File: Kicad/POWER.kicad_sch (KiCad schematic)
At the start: 0 parts

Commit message: power section
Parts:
- added C? (x2): 10uF, symbol Device:C_Small
- added C? (x2): 1u, symbol Device:C_Small
- added R?: 10k, symbol Device:R_Small
- added U?: TPS76718QD, D0008A_N, symbol project_sym_lib:TPS76718QD
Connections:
- new net GND: C?.2, C?.2, C?.2, C?.2, U?.1 (GND), U?.2 (EN_N)
- new net VDD_1V8: C?.1, C?.1, R?.2, U?.5 (OUT), U?.6 (OUT)
- new net V_BUCK: C?.1, C?.1, U?.3 (IN), U?.4 (IN)
- new net ~{RESET}: R?.1, U?.8 (RESET_N)
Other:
- note removed: "TODO: LDO 3V3"

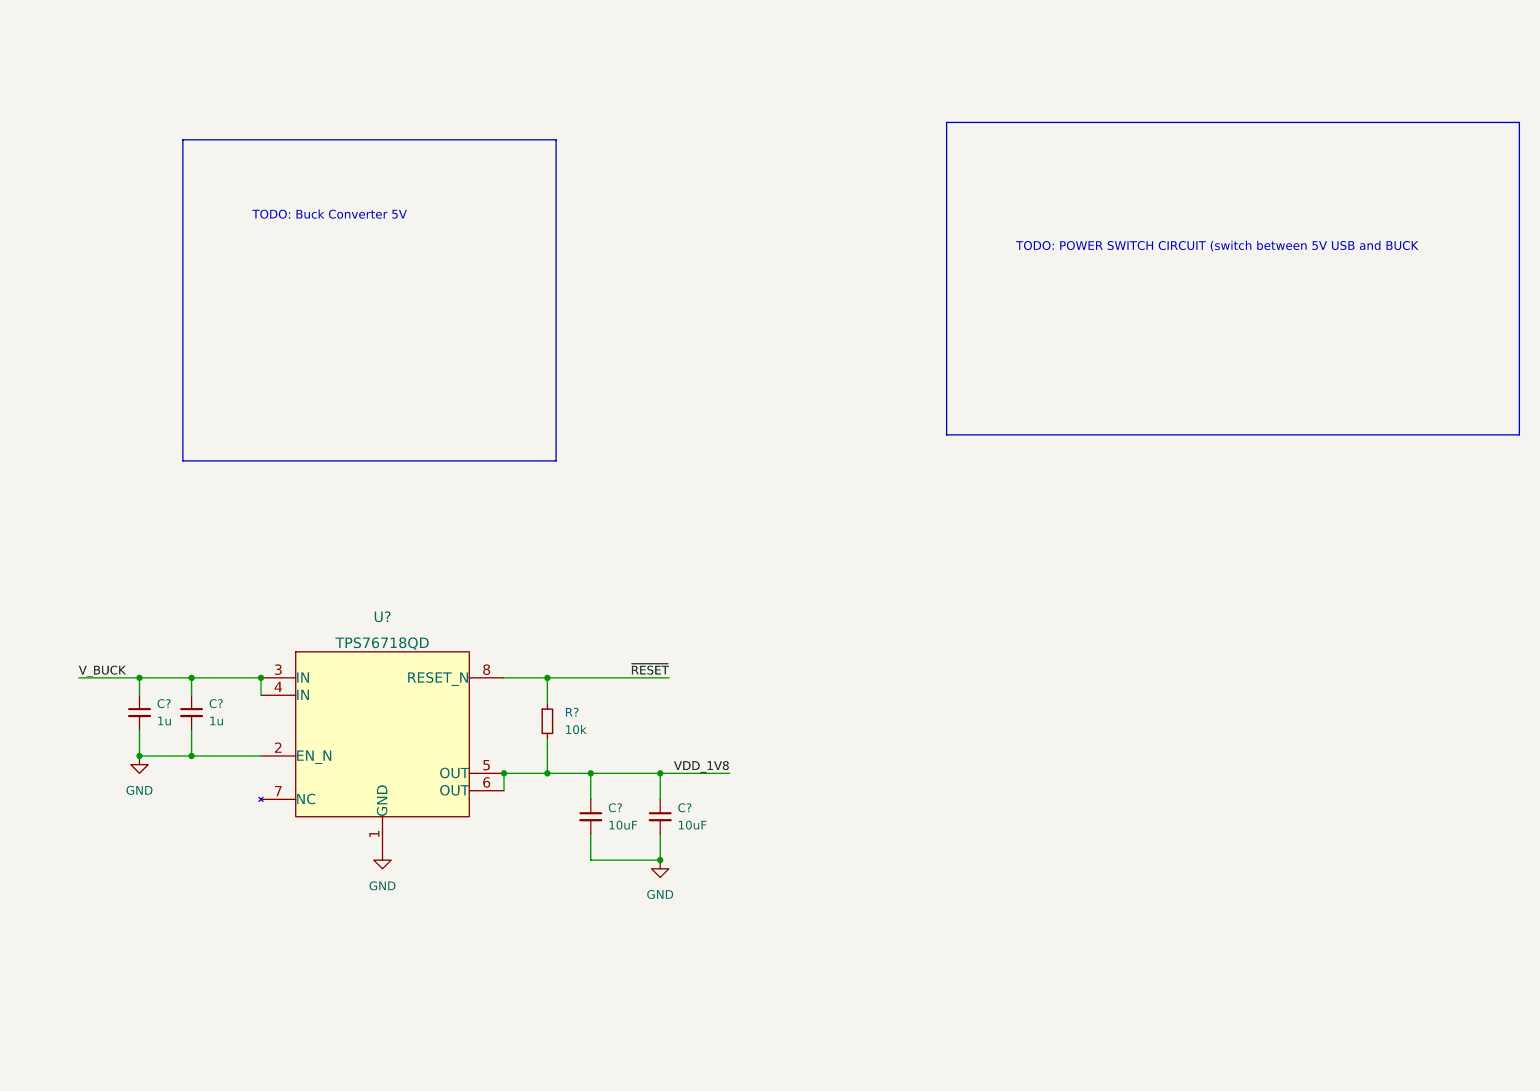
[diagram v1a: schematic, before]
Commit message: Basic Power layout done
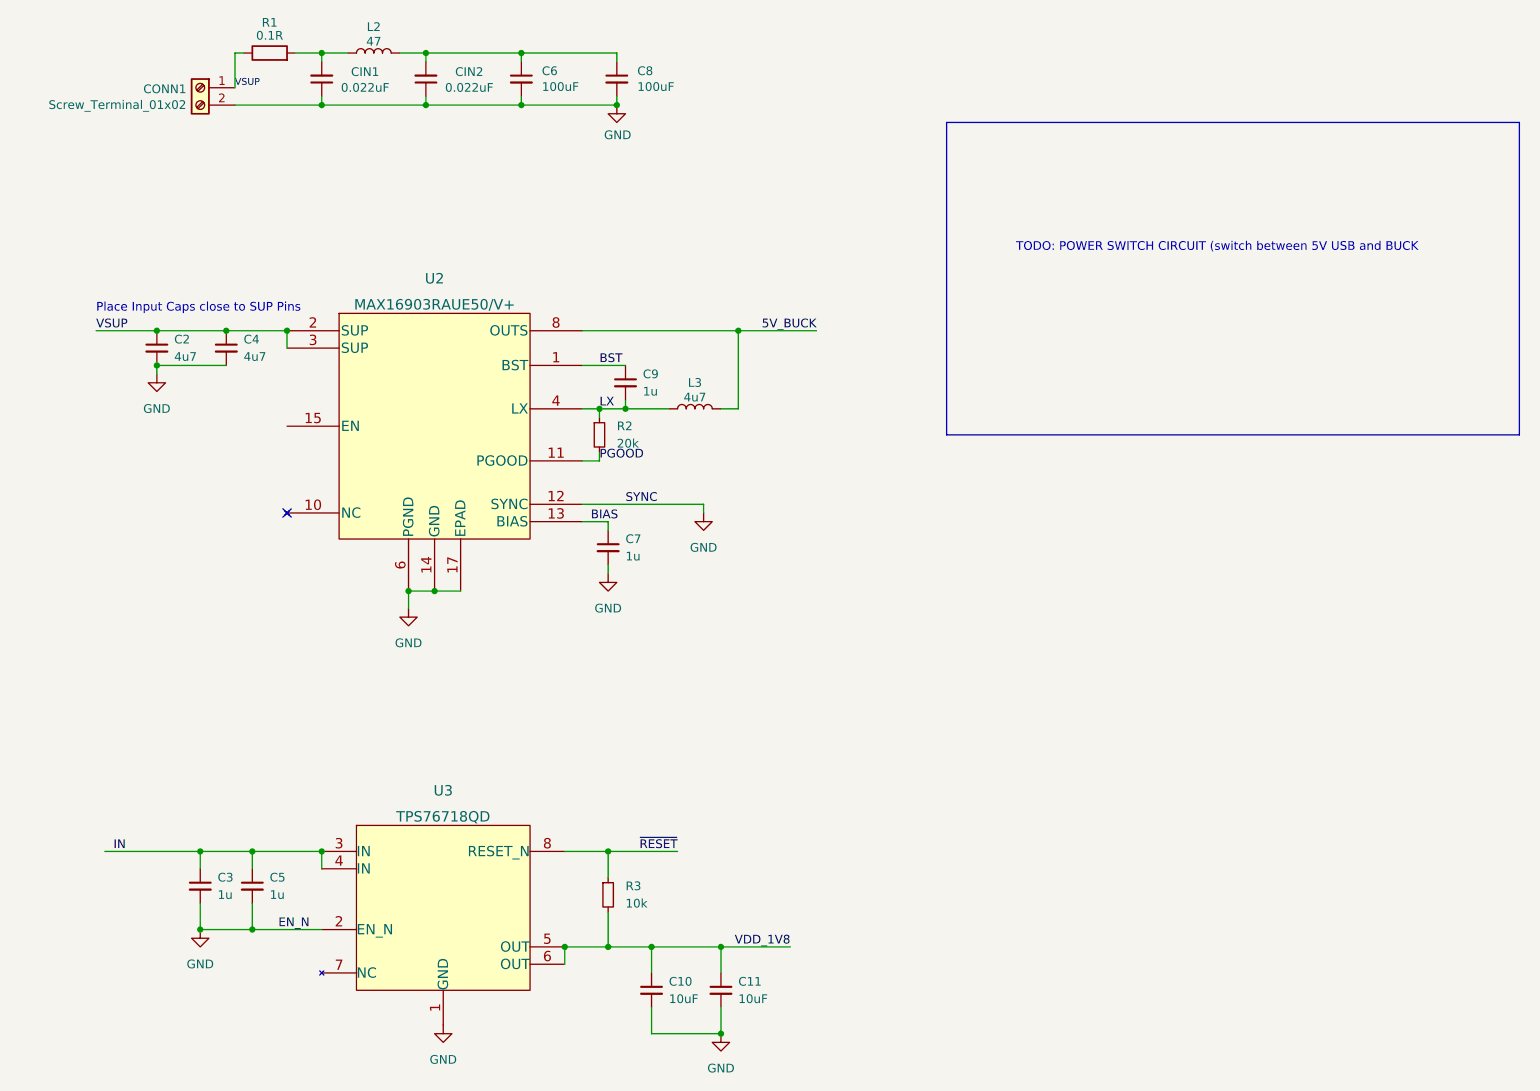
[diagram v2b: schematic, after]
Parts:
- added C2, C4: 4u7, Capacitor_SMD:C_0805_2012Metric, symbol Device:C_Small
- added C6, C8: 100uF, Capacitor_THT:CP_Radial_D10.0mm_P5.00mm, symbol Device:C_Small
- added C7, C9: 1u, Capacitor_SMD:C_0805_2012Metric, symbol Device:C_Small
- added CIN1, CIN2: 0.022uF, Capacitor_SMD:C_1206_3216Metric, symbol Device:C_Small
- added CONN1: Screw_Terminal_01x02, TerminalBlock_Phoenix:TerminalBlock_Phoenix_MKDS-1,5-2_1x02_P5.00mm_Horizontal, symbol Connector:Screw_Terminal_01x02
- added L2: 47, Inductor_SMD:L_2010_5025Metric, symbol Device:L
- added L3: 4u7, Inductor_SMD:L_2010_5025Metric, symbol Device:L
- added R1: 0.1R, Resistor_SMD:R_2512_6332Metric, symbol Device:R
- added R2: 20k, Resistor_SMD:R_0805_2012Metric, symbol Device:R_Small
- added U2: MAX16903RAUE50/V+, project_footprints:MAX16903RAUE50&slash_V&plus_, symbol project_sym_lib:MAX16903RAUE50/V+
- C10, C11, C3, C5: renamed from C?; footprint (none) -> Capacitor_SMD:C_0805_2012Metric
- R3: renamed from R?; footprint (none) -> Resistor_SMD:R_0805_2012Metric
- U3: renamed from U?; footprint D0008A_N -> project_footprints:TPS76718QD
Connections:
- net GND: now also C2.2, C4.2, C6.2, C7.2, C8.2, CIN1.1, CIN2.1, CONN1.2 (Pin_2), U2.12 (SYNC), U2.14 (GND), U2.17 (EPAD), U2.6 (PGND), U2.7 (PGND)
- net V_BUCK renamed IN
- new net: C6.1, C8.1, CIN2.2, L2.2
- new net: CIN1.2, L2.1, R1.2
- new net: U2.10 (NC), U2.16 (NC), U2.9 (NC)
- new net 5V_BUCK: L3.2, U2.8 (OUTS)
- new net BIAS: C7.1, U2.13 (BIAS)
- new net BST: C9.1, U2.1 (BST)
- new net LX: C9.2, L3.1, R2.1, U2.4 (LX), U2.5 (LX)
- new net PGOOD: R2.2, U2.11 (PGOOD)
- new net VSUP: C2.1, C4.1, CONN1.1 (Pin_1), R1.1, U2.2 (SUP), U2.3 (SUP)
- no-connect marks 0 -> 1
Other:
- note added: "Place Input Caps close to SUP Pins"
- note removed: "TODO: Buck Converter 5V"
- moved on the sheet: C10, C11, C3, C5, R3, U3

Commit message: moved Buck to external components sheet
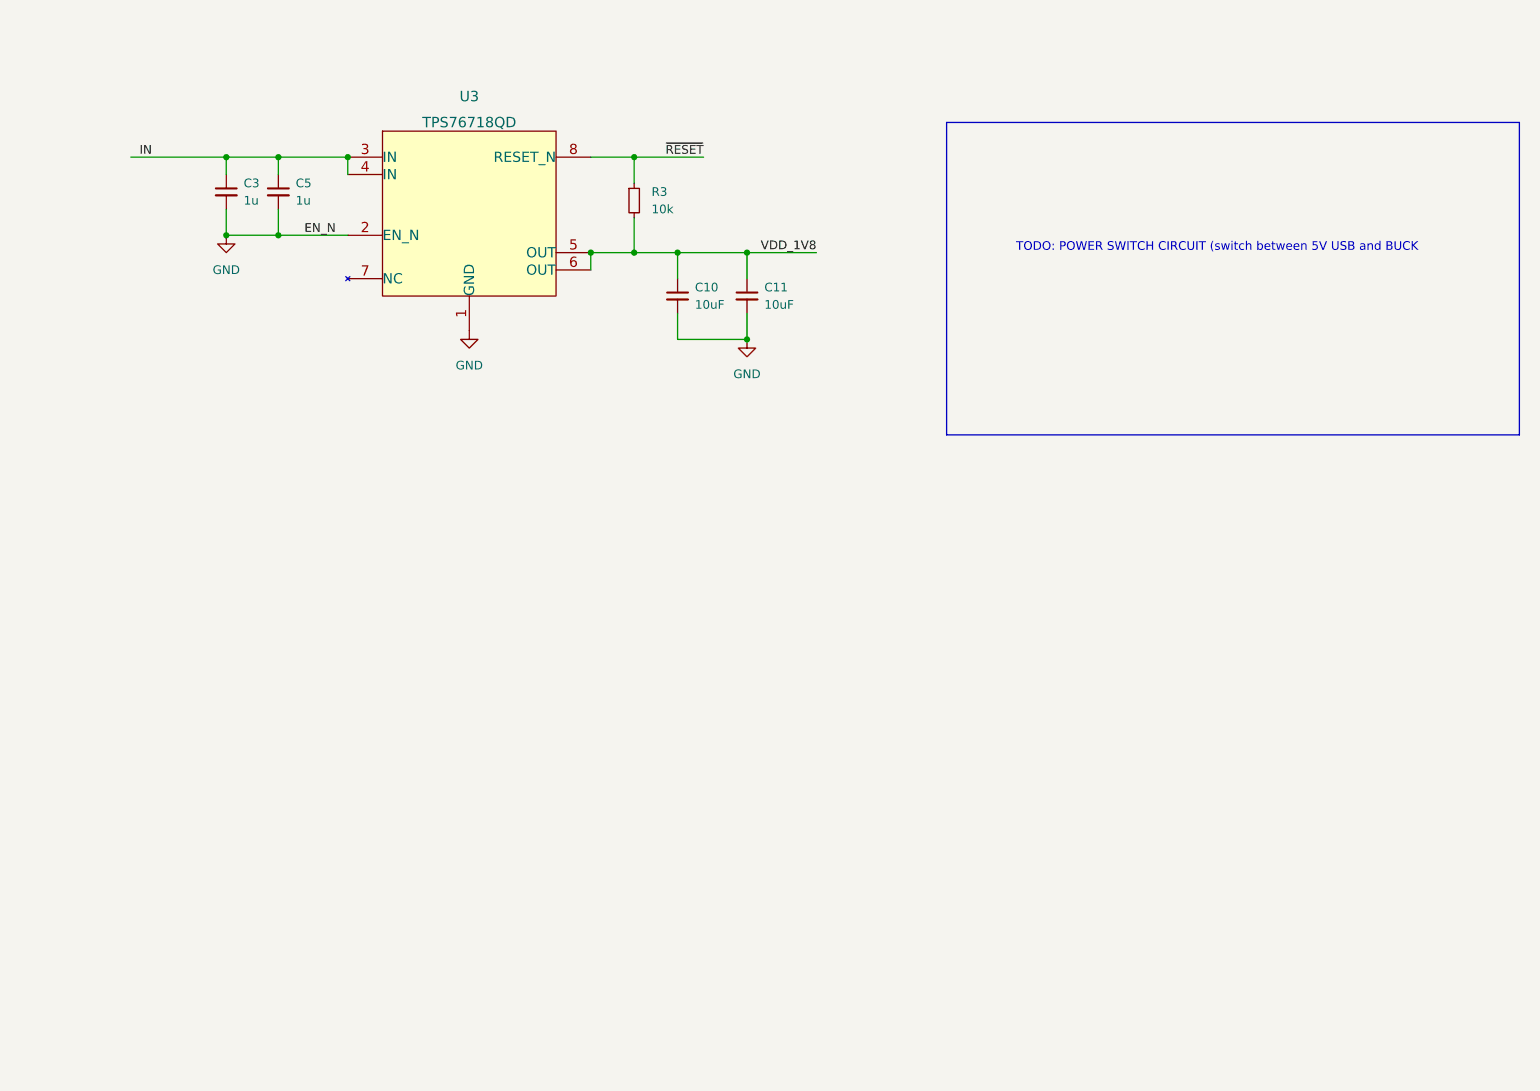
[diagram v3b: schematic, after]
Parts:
- removed C2, C4: 4u7, Capacitor_SMD:C_0805_2012Metric, symbol Device:C_Small
- removed C6, C8: 100uF, Capacitor_THT:CP_Radial_D10.0mm_P5.00mm, symbol Device:C_Small
- removed C7, C9: 1u, Capacitor_SMD:C_0805_2012Metric, symbol Device:C_Small
- removed CIN1, CIN2: 0.022uF, Capacitor_SMD:C_1206_3216Metric, symbol Device:C_Small
- removed CONN1: Screw_Terminal_01x02, TerminalBlock_Phoenix:TerminalBlock_Phoenix_MKDS-1,5-2_1x02_P5.00mm_Horizontal, symbol Connector:Screw_Terminal_01x02
- removed L2: 47, Inductor_SMD:L_2010_5025Metric, symbol Device:L
- removed L3: 4u7, Inductor_SMD:L_2010_5025Metric, symbol Device:L
- removed R1: 0.1R, Resistor_SMD:R_2512_6332Metric, symbol Device:R
- removed R2: 20k, Resistor_SMD:R_0805_2012Metric, symbol Device:R_Small
- removed U2: MAX16903RAUE50/V+, project_footprints:MAX16903RAUE50&slash_V&plus_, symbol project_sym_lib:MAX16903RAUE50/V+
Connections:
- no-connect marks 1 -> 0
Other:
- note removed: "Place Input Caps close to SUP Pins"
- moved on the sheet: C10, C11, C3, C5, R3, U3

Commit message: working on DSP
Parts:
- renumbered C3 to C2, C5 to C3, C10 to C4, C11 to C5, R3 to R1, U3 to U2
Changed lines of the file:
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@@
   (symbol (lib_id "Device:C_Small") (at 119.38 66.04 0) (unit 1)
     (in_bom yes) (on_board yes) (fields_autoplaced)
-    (property "Reference" "C10" (id 0) (at 121.92 64.7762 0)
+    (property "Reference" "C4" (id 0) (at 121.92 64.7762 0)
       (effects (font (size 1.27 1.27)) (justify left))
     )
@@
   (symbol (lib_id "Device:C_Small") (at 129.54 66.04 0) (unit 1)
     (in_bom yes) (on_board yes) (fields_autoplaced)
-    (property "Reference" "C11" (id 0) (at 132.08 64.7762 0)
+    (property "Reference" "C5" (id 0) (at 132.08 64.7762 0)
       (effects (font (size 1.27 1.27)) (justify left))
     )
@@
   (symbol (lib_id "Device:C_Small") (at 53.34 50.8 0) (unit 1)
     (in_bom yes) (on_board yes) (fields_autoplaced)
-    (property "Reference" "C3" (id 0) (at 55.88 49.5362 0)
+    (property "Reference" "C2" (id 0) (at 55.88 49.5362 0)
       (effects (font (size 1.27 1.27)) (justify left))
     )
@@
   (symbol (lib_id "Device:R_Small") (at 113.03 52.07 0) (unit 1)
     (in_bom yes) (on_board yes) (fields_autoplaced)
-    (property "Reference" "R3" (id 0) (at 115.57 50.7999 0)
+    (property "Reference" "R1" (id 0) (at 115.57 50.7999 0)
       (effects (font (size 1.27 1.27)) (justify left))
     )
@@
   (symbol (lib_id "power:GND") (at 129.54 72.39 0) (unit 1)
     (in_bom yes) (on_board yes) (fields_autoplaced)
-    (property "Reference" "#PWR016" (id 0) (at 129.54 78.74 0)
+    (property "Reference" "#PWR011" (id 0) (at 129.54 78.74 0)
       (effects (font (size 1.27 1.27)) hide)
     )
@@
   (symbol (lib_id "project_sym_lib:TPS76718QD") (at 88.9 53.34 0) (unit 1)
     (in_bom yes) (on_board yes) (fields_autoplaced)
-    (property "Reference" "U3" (id 0) (at 88.9 36.83 0)
+    (property "Reference" "U2" (id 0) (at 88.9 36.83 0)
       (effects (font (size 1.524 1.524)))
     )
@@
   (symbol (lib_id "power:GND") (at 88.9 71.12 0) (unit 1)
     (in_bom yes) (on_board yes) (fields_autoplaced)
-    (property "Reference" "#PWR012" (id 0) (at 88.9 77.47 0)
+    (property "Reference" "#PWR010" (id 0) (at 88.9 77.47 0)
       (effects (font (size 1.27 1.27)) hide)
     )
@@
   (symbol (lib_id "Device:C_Small") (at 60.96 50.8 0) (unit 1)
     (in_bom yes) (on_board yes) (fields_autoplaced)
-    (property "Reference" "C5" (id 0) (at 63.5 49.5362 0)
+    (property "Reference" "C3" (id 0) (at 63.5 49.5362 0)
       (effects (font (size 1.27 1.27)) (justify left))
     )
@@
   (symbol (lib_id "power:GND") (at 53.34 57.15 0) (unit 1)
     (in_bom yes) (on_board yes) (fields_autoplaced)
-    (property "Reference" "#PWR010" (id 0) (at 53.34 63.5 0)
+    (property "Reference" "#PWR09" (id 0) (at 53.34 63.5 0)
       (effects (font (size 1.27 1.27)) hide)
     )
